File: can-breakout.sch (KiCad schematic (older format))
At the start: 9 parts, among them J1 Screw_Terminal_01x02, J2 Conn_01x05, J3 Screw_Terminal_01x02, U1 SN65HVD256

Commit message: Start work on CAN layout
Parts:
- J2: footprint (none) -> breakout:M20-7890546
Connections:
- no-connect marks 1 -> 0
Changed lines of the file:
@@
 F 0 "J2" H 2880 4160 50  0000 C CNN
 F 1 "Conn_01x05" H 2880 3560 50  0000 C CNN
-F 2 "" H 2880 3860 50  0001 C CNN
+F 2 "breakout:M20-7890546" H 2880 3860 50  0001 C CNN
 F 3 "http://www.mouser.com/ds/2/181/M20-789-1132299.pdf" H 2880 3860 50  0001 C CNN
 	1    2880 3860
@@
 	3740 4260 3610 4260
 Connection ~ 3610 4260
-NoConn ~ 2860 3830
 $EndSCHEMATC

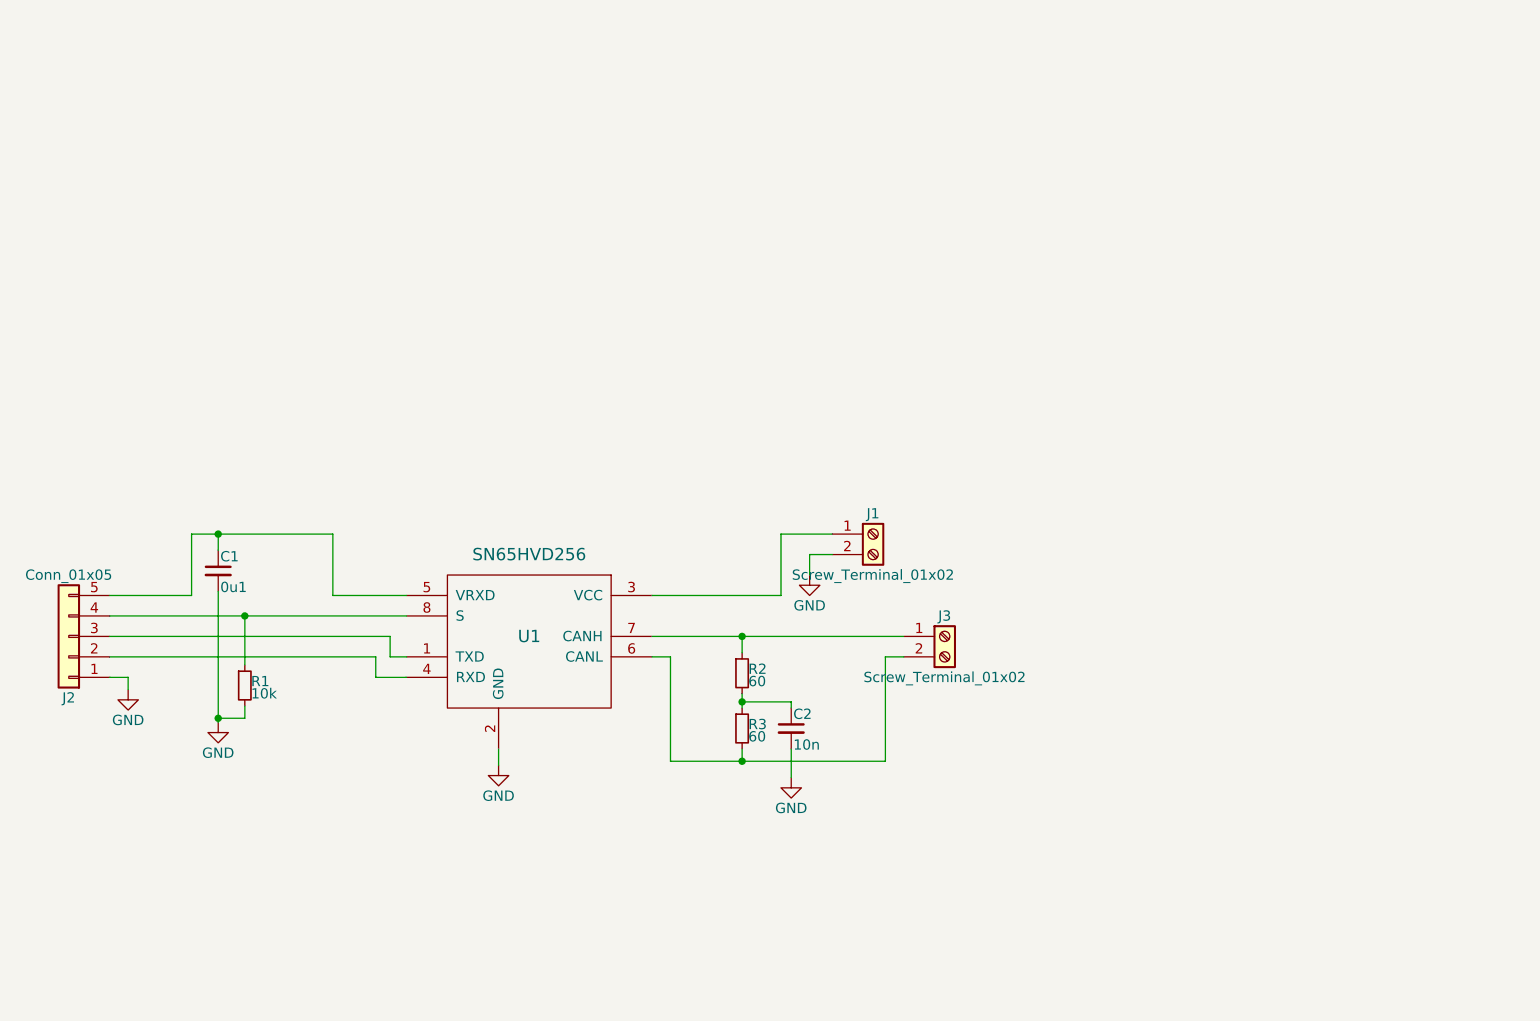
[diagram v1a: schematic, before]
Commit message: Make library files for both connectors and wire them together
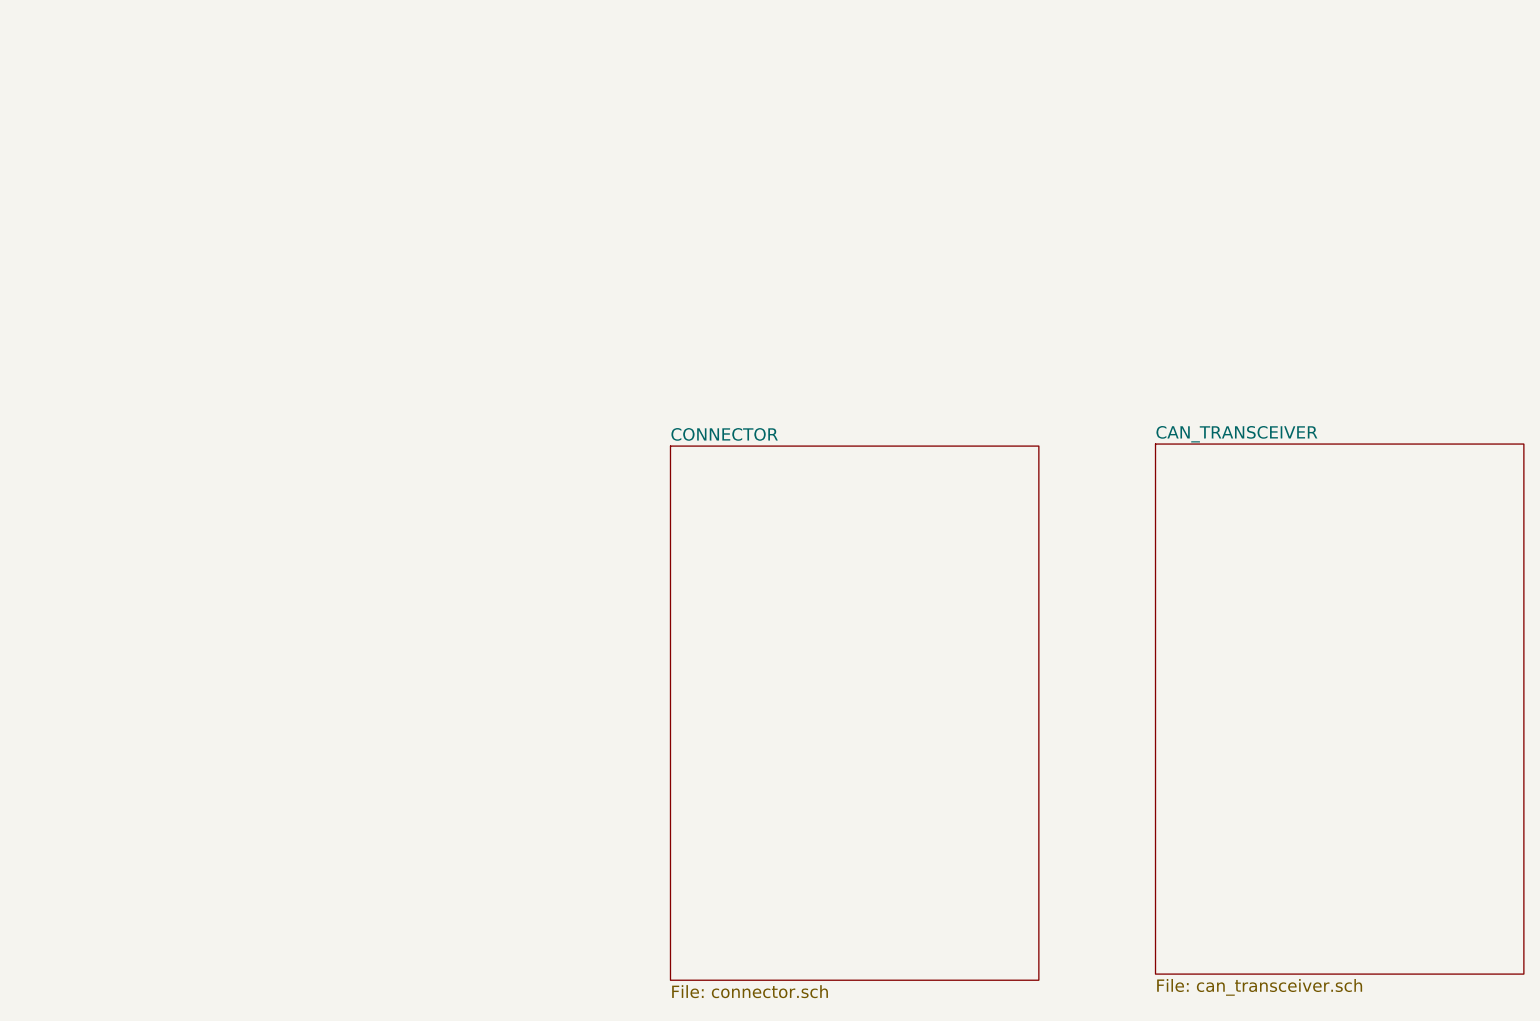
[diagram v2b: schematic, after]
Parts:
- removed C1: 0u1, Capacitors_SMD:C_0805_HandSoldering, symbol C_Small
- removed C2: 10n, Capacitors_SMD:C_0805_HandSoldering, symbol C_Small
- removed J1, J3: Screw_Terminal_01x02, breakout:1729128, symbol Screw_Terminal_01x02
- removed J2: Conn_01x05, breakout:M20-7890546, symbol Conn_01x05
- removed R1: 10k, Resistors_SMD:R_0805_HandSoldering, symbol R_Small
- removed R2, R3: 60, Resistors_SMD:R_1206_HandSoldering, symbol R_Small
- removed U1: SN65HVD256, breakout:TI_SOIC8, symbol SN65HVD256

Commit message: Add some protection diodes, connect most things up TODO add TVS diodes to CAN bus terinals
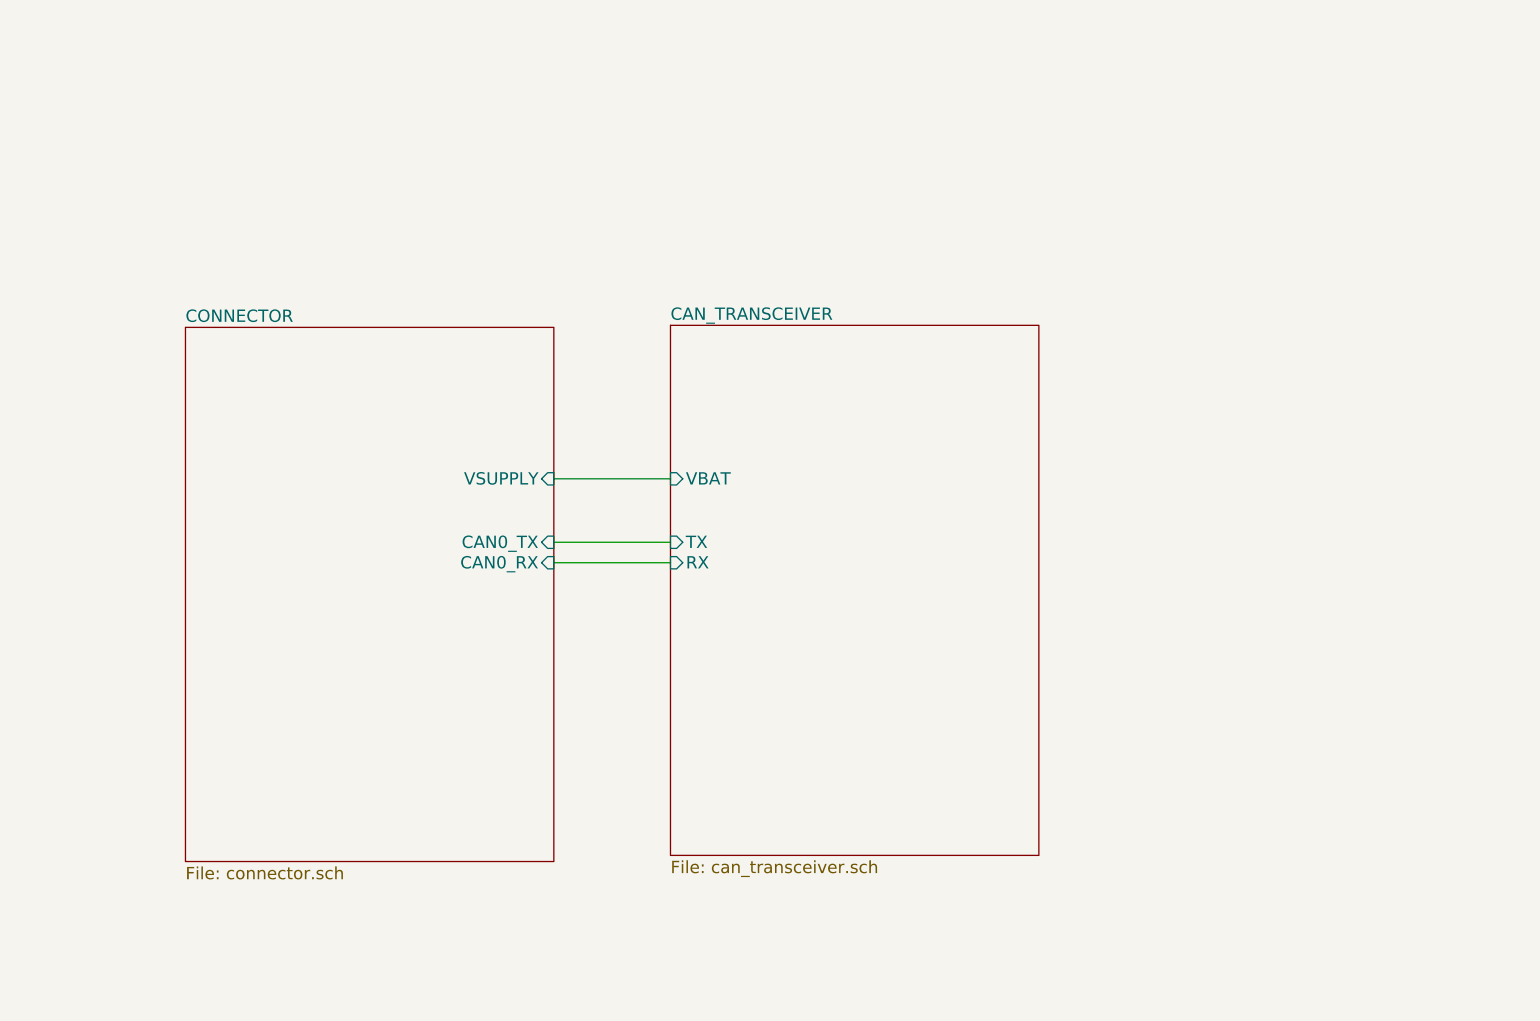
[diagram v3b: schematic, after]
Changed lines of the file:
@@
 LIBS:sn65hvd256
 LIBS:samtec
+LIBS:mic5365-33yd5-tr
 LIBS:can-breakout-cache
 EELAYER 25 0
@@
 $EndDescr
 $Sheet
-S 8190 2920 1800 2590
+S 5820 2340 1800 2590
 U 5A128056
 F0 "CAN_TRANSCEIVER" 60
 F1 "can_transceiver.sch" 60
+F2 "TX" I L 5820 3400 60
+F3 "RX" I L 5820 3500 60
+F4 "VBAT" I L 5820 3090 60
 $EndSheet
 $Sheet
-S 5820 2930 1800 2610
+S 3450 2350 1800 2610
 U 5A129041
 F0 "CONNECTOR" 60
 F1 "connector.sch" 60
+F2 "CAN0_TX" I R 5250 3400 60
+F3 "CAN0_RX" I R 5250 3500 60
+F4 "VSUPPLY" I R 5250 3090 60
 $EndSheet
+Wire Wire Line
+	5250 3090 5820 3090
+Wire Wire Line
+	5820 3400 5250 3400
+Wire Wire Line
+	5250 3500 5820 3500
 $EndSCHEMATC

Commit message: Parts laid out, only routing left
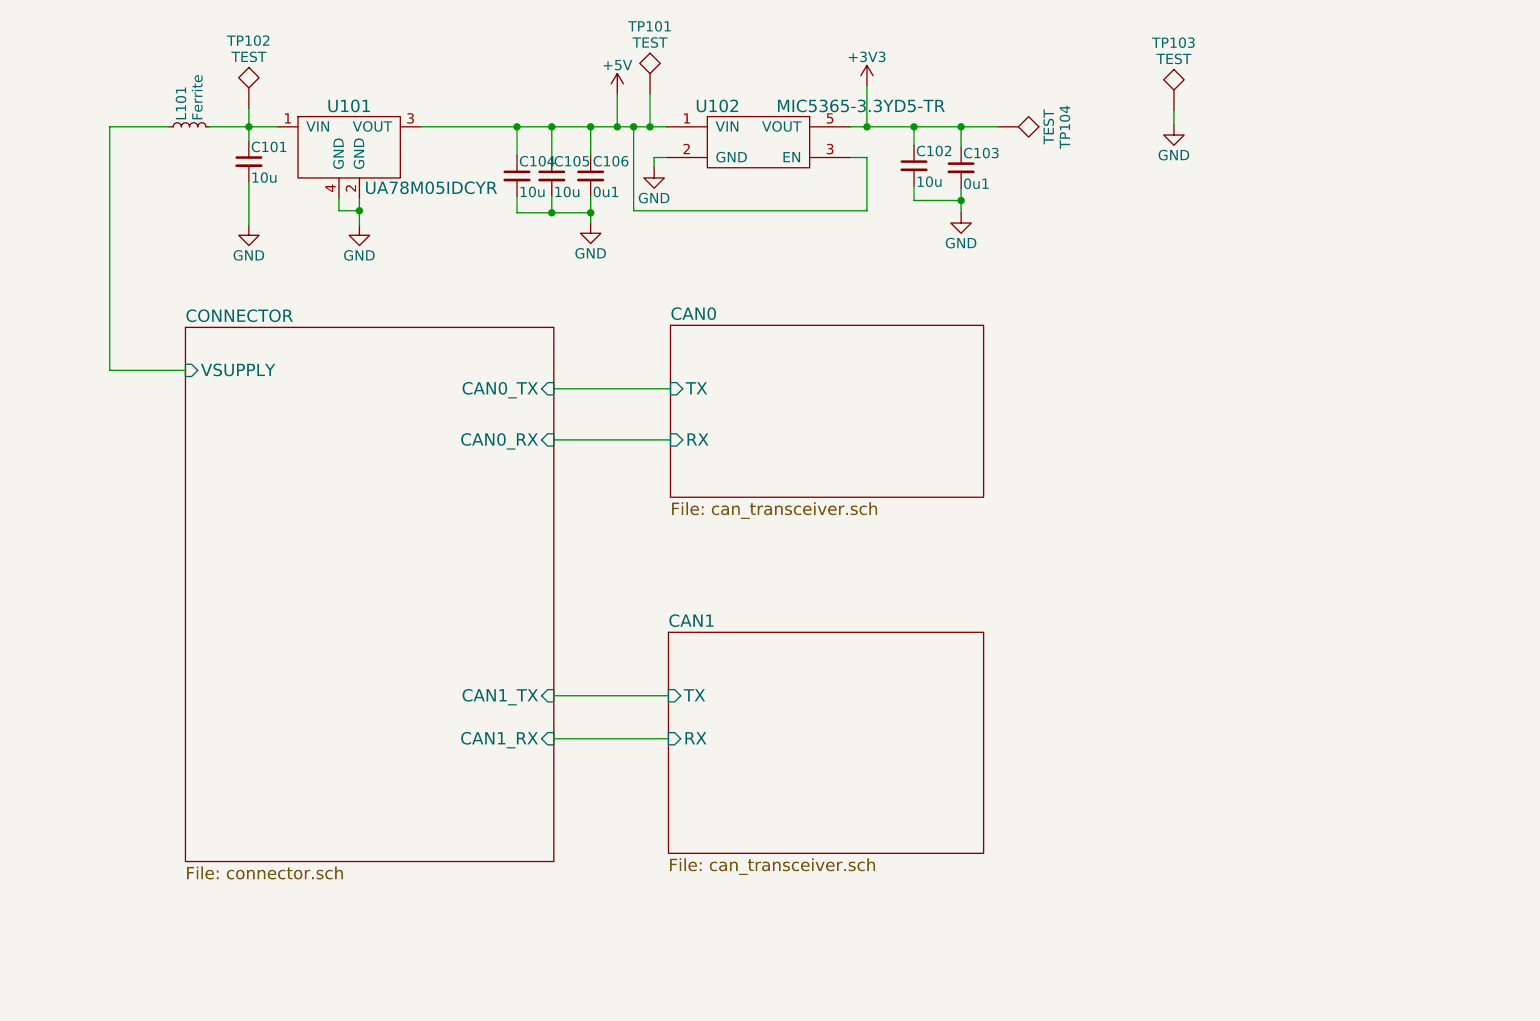
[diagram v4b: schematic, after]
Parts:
- added C101, C102, C104, C105: 10u, Capacitors_SMD:C_1206_HandSoldering, symbol C_Small
- added C103, C106: 0u1, Capacitors_SMD:C_1206_HandSoldering, symbol C_Small
- added L101: Ferrite, Resistors_SMD:R_1206_HandSoldering, symbol L_Small
- added TP101, TP102, TP103, TP104: TEST, Measurement_Points:Measurement_Point_Round-SMD-Pad_Small, symbol TEST
- added U101: UA78M05IDCYR, breakout:TI_SOT-223-4, symbol UA78M05IDCYR
- added U102: MIC5365-3.3YD5-TR, TO_SOT_Packages_SMD:SOT-23-5, symbol MIC5365-3.3YD5-TR
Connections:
- new net: C101.1, L101.2, TP102.1, U101.1 (VIN)
- new net +3V3: C102.1, C103.1, TP104.1, U102.5 (VOUT)
- new net +5V: C104.1, C105.1, C106.1, TP101.1, U101.3 (VOUT), U102.1 (VIN), U102.3 (EN)
- new net CONNECTOR/VSUPPLY: L101.1
- new net GND: C101.2, C102.2, C103.2, C104.2, C105.2, C106.2, TP103.1, U101.2 (GND), U101.4 (GND), U102.2 (GND)
